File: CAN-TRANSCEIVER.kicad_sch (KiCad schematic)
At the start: 15 parts, among them IC2 ATA6561-GAQW-N

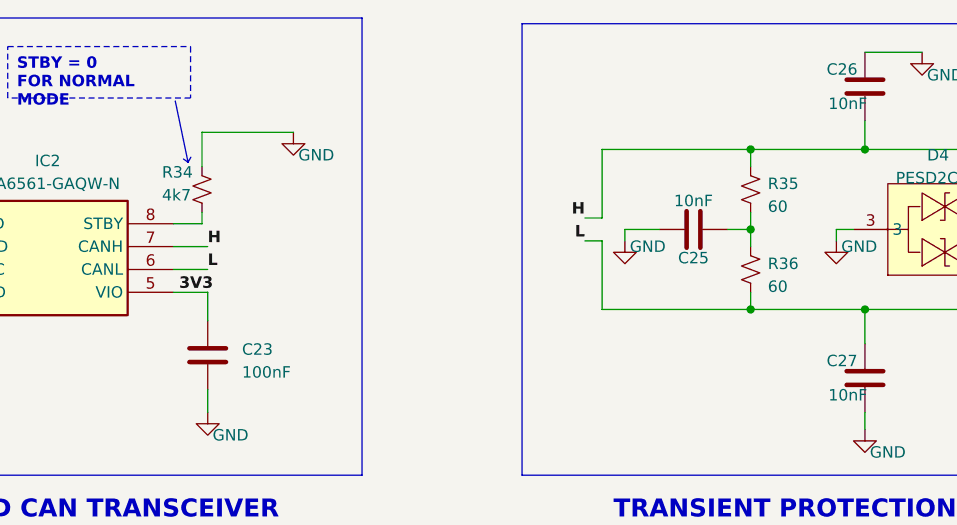
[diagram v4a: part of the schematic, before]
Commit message: Assigned footprints
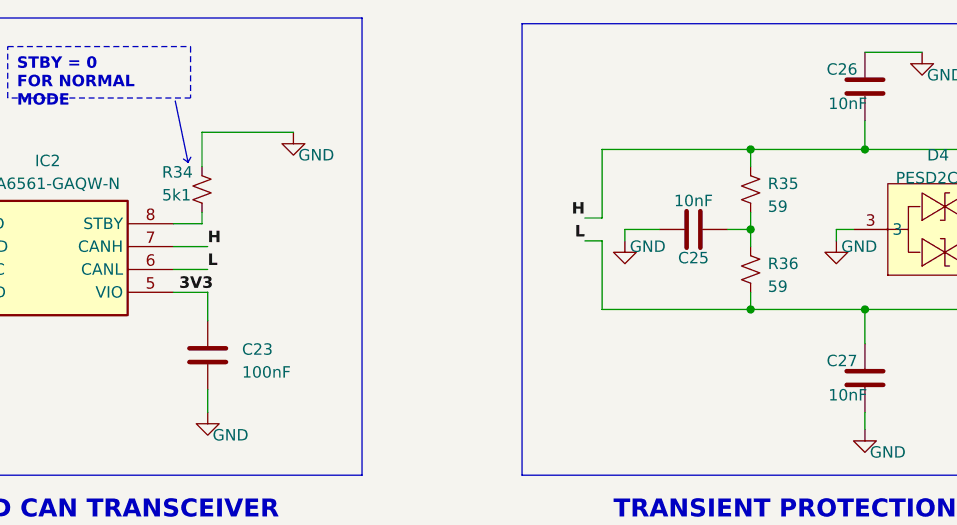
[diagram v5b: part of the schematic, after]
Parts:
- C23, C24, C25, C26, C27: footprint ESP32-S3_DB:C_0402_1005Metric -> ESP32-S3_Dev_Board:C_0402_1005Metric
- D4: footprint easyeda2kicad:SOT-23-3_L2.9-W1.3-P1.90-LS2.4-BR -> ESP32-S3_Dev_Board:SOT-23-3; PN (none) -> PESD2CAN
- IC2: footprint SOIC127P600X175-8N -> ESP32-S3_Dev_Board:SOP-8_3.9x4.9mm_P1.27mm; PN (none) -> ATA6561-GAQW-N
- R14: footprint (none) -> ESP32-S3_Dev_Board:R_0603_1608Metric; PN (none) -> RC0603JR-070RL
- R34: value 4k7 -> 5k1; footprint (none) -> ESP32-S3_Dev_Board:R_0402_1005Metric; PN (none) -> RC0402FR-075K1L
- R35, R36: value 60 -> 59; footprint (none) -> ESP32-S3_Dev_Board:R_0402_1005Metric; PN (none) -> RC0402FR-0759RL
- R37, R38: footprint (none) -> ESP32-S3_Dev_Board:R_0402_1005Metric; PN (none) -> RTT02100JTH
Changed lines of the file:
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@@
       (effects (font (size 1.27 1.27)) (justify left))
     )
-    (property "Footprint" "ESP32-S3_DB:C_0402_1005Metric" (at 167.3352 114.3 0)
+    (property "Footprint" "ESP32-S3_Dev_Board:C_0402_1005Metric" (at 167.3352 114.3 0)
       (effects (font (size 1.27 1.27)) hide)
     )
@@
       (effects (font (size 1.27 1.27)) (justify right))
     )
-    (property "Footprint" "ESP32-S3_DB:C_0402_1005Metric" (at 124.1552 106.68 0)
+    (property "Footprint" "ESP32-S3_Dev_Board:C_0402_1005Metric" (at 124.1552 106.68 0)
       (effects (font (size 1.27 1.27)) hide)
     )
@@
       (effects (font (size 1.27 1.27)) (justify right))
     )
-    (property "Value" "4k7" (at 161.29 92.71 0)
-      (effects (font (size 1.27 1.27)) (justify right))
-    )
-    (property "Footprint" "" (at 165.735 92.075 0)
+    (property "Value" "5k1" (at 161.29 92.71 0)
+      (effects (font (size 1.27 1.27)) (justify right))
+    )
+    (property "Footprint" "ESP32-S3_Dev_Board:R_0402_1005Metric" (at 165.735 92.075 0)
       (effects (font (size 1.27 1.27)) hide)
     )
@@
       (effects (font (size 1.27 1.27)) hide)
     )
+    (property "PN" "RC0402FR-075K1L" (at 165.735 92.075 0)
+      (effects (font (size 1.27 1.27)) hide)
+    )
     (pin "1")
     (pin "2")
@@
       (effects (font (size 1.27 1.27)))
     )
-    (property "Footprint" "ESP32-S3_DB:C_0402_1005Metric" (at 238.4298 76.835 0)
+    (property "Footprint" "ESP32-S3_Dev_Board:C_0402_1005Metric" (at 238.4298 76.835 0)
       (effects (font (size 1.27 1.27)) hide)
     )
@@
       (effects (font (size 1.27 1.27)))
     )
-    (property "Footprint" "" (at 131.445 100.965 0)
+    (property "Footprint" "ESP32-S3_Dev_Board:R_0603_1608Metric" (at 131.445 100.965 0)
       (effects (font (size 1.27 1.27)) hide)
     )
     (property "Datasheet" "~" (at 131.445 100.965 0)
+      (effects (font (size 1.27 1.27)) hide)
+    )
+    (property "PN" "RC0603JR-070RL" (at 131.445 100.965 0)
       (effects (font (size 1.27 1.27)) hide)
     )
@@
       (effects (font (size 1.27 1.27)) (justify right))
     )
-    (property "Value" "60" (at 228.6 102.87 0)
-      (effects (font (size 1.27 1.27)) (justify right))
-    )
-    (property "Footprint" "" (at 226.695 100.965 0)
+    (property "Value" "59" (at 228.6 102.87 0)
+      (effects (font (size 1.27 1.27)) (justify right))
+    )
+    (property "Footprint" "ESP32-S3_Dev_Board:R_0402_1005Metric" (at 226.695 100.965 0)
       (effects (font (size 1.27 1.27)) hide)
     )
     (property "Datasheet" "~" (at 226.695 100.965 0)
+      (effects (font (size 1.27 1.27)) hide)
+    )
+    (property "PN" "RC0402FR-0759RL" (at 226.695 100.965 0)
       (effects (font (size 1.27 1.27)) hide)
     )
@@
       (effects (font (size 1.27 1.27)))
     )
-    (property "Footprint" "SOIC127P600X175-8N" (at 158.75 190.805 0)
+    (property "Footprint" "ESP32-S3_Dev_Board:SOP-8_3.9x4.9mm_P1.27mm" (at 158.75 190.805 0)
       (effects (font (size 1.27 1.27)) (justify left top) hide)
     )
@@
     (property "Arrow Price/Stock" "https://www.arrow.com/en/products/ata6561-gaqw-n/microchip-technology?region=nac" (at 158.75 1090.805 0)
       (effects (font (size 1.27 1.27)) (justify left top) hide)
+    )
+    (property "PN" "ATA6561-GAQW-N" (at 134.62 95.885 0)
+      (effects (font (size 1.27 1.27)) hide)
     )
     (pin "1")
@@
       (effects (font (size 1.27 1.27)))
     )
-    (property "Footprint" "easyeda2kicad:SOT-23-3_L2.9-W1.3-P1.90-LS2.4-BR" (at 263.525 96.52 0)
+    (property "Footprint" "ESP32-S3_Dev_Board:SOT-23-3" (at 263.525 96.52 0)
       (effects (font (size 1.27 1.27)) hide)
     )
@@
     )
     (property "LCSC Part" "C284078" (at 268.605 96.52 0)
+      (effects (font (size 1.27 1.27)) hide)
+    )
+    (property "PN" "PESD2CAN" (at 248.285 96.52 0)
       (effects (font (size 1.27 1.27)) hide)
     )
@@
       (effects (font (size 1.27 1.27)) (justify right))
     )
-    (property "Footprint" "" (at 66.04 101.6 0)
+    (property "Footprint" "ESP32-S3_Dev_Board:R_0402_1005Metric" (at 66.04 101.6 0)
       (effects (font (size 1.27 1.27)) hide)
     )
@@
       (effects (font (size 1.27 1.27)) hide)
     )
+    (property "PN" "RTT02100JTH" (at 66.04 101.6 0)
+      (effects (font (size 1.27 1.27)) hide)
+    )
     (pin "1")
     (pin "2")
@@
       (effects (font (size 1.27 1.27)) (justify right))
     )
-    (property "Footprint" "" (at 66.04 95.25 0)
+    (property "Footprint" "ESP32-S3_Dev_Board:R_0402_1005Metric" (at 66.04 95.25 0)
       (effects (font (size 1.27 1.27)) hide)
     )
     (property "Datasheet" "~" (at 66.04 95.25 0)
+      (effects (font (size 1.27 1.27)) hide)
+    )
+    (property "PN" "RTT02100JTH" (at 66.04 95.25 0)
       (effects (font (size 1.27 1.27)) hide)
     )
@@
       (effects (font (size 1.27 1.27)) (justify right))
     )
-    (property "Value" "60" (at 228.6 93.98 0)
-      (effects (font (size 1.27 1.27)) (justify right))
-    )
-    (property "Footprint" "" (at 226.695 92.075 0)
+    (property "Value" "59" (at 228.6 93.98 0)
+      (effects (font (size 1.27 1.27)) (justify right))
+    )
+    (property "Footprint" "ESP32-S3_Dev_Board:R_0402_1005Metric" (at 226.695 92.075 0)
       (effects (font (size 1.27 1.27)) hide)
     )
@@
       (effects (font (size 1.27 1.27)) hide)
     )
+    (property "PN" "RC0402FR-0759RL" (at 226.695 92.075 0)
+      (effects (font (size 1.27 1.27)) hide)
+    )
     (pin "1")
     (pin "2")
@@
       (effects (font (size 1.27 1.27)))
     )
-    (property "Footprint" "ESP32-S3_DB:C_0402_1005Metric" (at 224.155 95.5548 0)
+    (property "Footprint" "ESP32-S3_Dev_Board:C_0402_1005Metric" (at 224.155 95.5548 0)
       (effects (font (size 1.27 1.27)) hide)
     )
@@
       (effects (font (size 1.27 1.27)))
     )
-    (property "Footprint" "ESP32-S3_DB:C_0402_1005Metric" (at 238.4298 109.22 0)
-      (effects (font (size 1.27 1.27)) hide)
-    )
+    (property "Footprint" "ESP32-S3_Dev_Board:C_0402_1005Metric" (at 238.4298 109.22 0)
+      (effects (font (size 1.27 1.27)) hide)
+    )

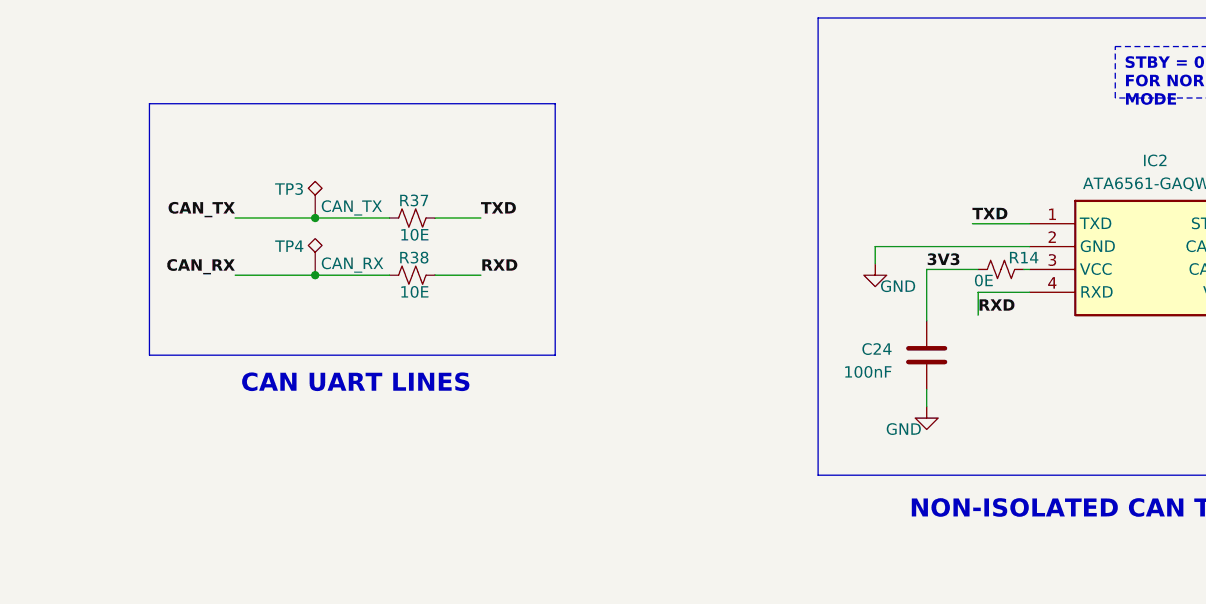
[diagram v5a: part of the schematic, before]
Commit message: Placed RS-485, CAN Transceiver and battery charger
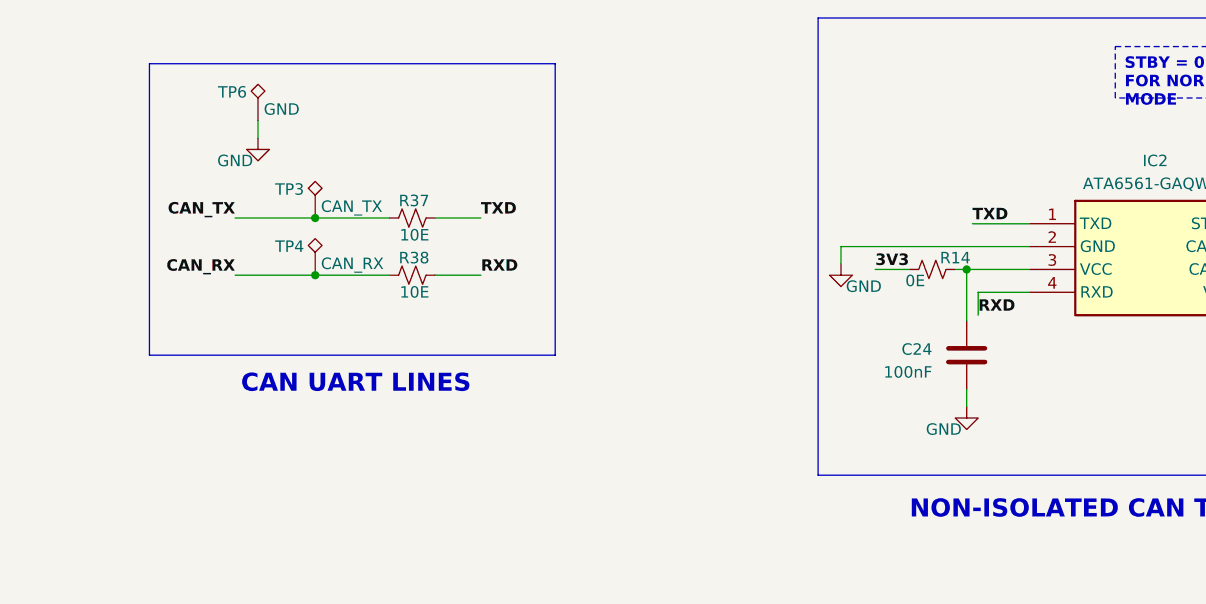
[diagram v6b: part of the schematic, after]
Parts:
- added TP6: GND, ESP32-S3_Dev_Board:Test_Pad_1.5mm, symbol ESP32-S3_DB:TestPoint_Alt
- TP3, TP4: footprint (none) -> ESP32-S3_Dev_Board:Test_Pad_1.5mm
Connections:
- net 3V3: no longer C24.2
- net GND: now also TP6.1
- net at IC2.3 (VCC), R14.2: now also C24.2
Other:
- moved on the sheet: C24, R14
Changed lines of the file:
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@@
   (junction (at 239.395 105.41) (diameter 0) (color 0 0 0 0)
   )
+  (junction (at 127.635 100.965) (diameter 0) (color 0 0 0 0)
+  )
   (junction (at 226.695 105.41) (diameter 0) (color 0 0 0 0)
   )
@@
     (stroke (width 1) (type default) (color 72 72 72 1))
   )
-  (wire (pts (xy 123.19 100.965) (xy 128.905 100.965))
+  (wire (pts (xy 117.475 100.965) (xy 121.285 100.965))
     (stroke (width 0) (type default))
   )
@@
     (stroke (width 0) (type default))
   )
-  (wire (pts (xy 123.19 114.3) (xy 123.19 116.205))
+  (wire (pts (xy 127.635 114.3) (xy 127.635 116.205))
     (stroke (width 0) (type default))
   )
@@
     (stroke (width 0) (type default))
   )
-  (bus (pts (xy 81.915 82.55) (xy 81.915 110.49))
+  (bus (pts (xy 81.915 78.105) (xy 81.915 110.49))
     (stroke (width 1) (type default) (color 72 72 72 1))
   )
@@
     (stroke (width 0) (type default))
   )
-  (wire (pts (xy 117.475 98.425) (xy 134.62 98.425))
+  (wire (pts (xy 113.665 98.425) (xy 134.62 98.425))
     (stroke (width 0) (type default))
   )
@@
     (stroke (width 0) (type default))
   )
-  (wire (pts (xy 133.985 100.965) (xy 134.62 100.965))
-    (stroke (width 0) (type default))
-  )
   (polyline (pts (xy 163.6776 88.6968) (xy 164.1856 89.0524))
     (stroke (width 0) (type default))
@@
     (stroke (width 0) (type default))
   )
-  (bus (pts (xy 36.83 82.55) (xy 81.915 82.55))
+  (bus (pts (xy 36.83 78.105) (xy 81.915 78.105))
     (stroke (width 1) (type default) (color 72 72 72 1))
   )
@@
     (stroke (width 0.5) (type default) (color 255 0 0 1))
   )
-  (bus (pts (xy 36.83 82.55) (xy 36.83 110.49))
+  (bus (pts (xy 36.83 78.105) (xy 36.83 110.49))
     (stroke (width 1) (type default) (color 72 72 72 1))
   )
@@
     (stroke (width 1) (type default) (color 72 72 72 1))
   )
-  (wire (pts (xy 117.475 100.33) (xy 117.475 98.425))
+  (wire (pts (xy 113.665 100.33) (xy 113.665 98.425))
     (stroke (width 0) (type default))
   )
@@
     (stroke (width 0) (type default))
   )
-  (wire (pts (xy 123.19 100.965) (xy 123.19 106.68))
+  (wire (pts (xy 127.635 100.965) (xy 134.62 100.965))
+    (stroke (width 0) (type default))
+  )
+  (wire (pts (xy 127.635 100.965) (xy 127.635 106.68))
     (stroke (width 0) (type default))
   )
@@
     (stroke (width 0) (type default))
   )
+  (wire (pts (xy 126.365 100.965) (xy 127.635 100.965))
+    (stroke (width 0) (type default))
+  )
   (wire (pts (xy 210.185 105.41) (xy 226.695 105.41))
     (stroke (width 0) (type default))
   )
   (wire (pts (xy 208.28 95.25) (xy 210.185 95.25))
+    (stroke (width 0) (type default))
+  )
+  (wire (pts (xy 48.895 86.36) (xy 48.895 84.455))
     (stroke (width 0) (type default))
   )
@@
     (effects (font (size 1.27 1.27) bold (color 0 0 255 1)) (justify left bottom))
   )
-  (label "3V3" (at 123.19 100.965 0) (fields_autoplaced)
+  (label "3V3" (at 117.475 100.965 0) (fields_autoplaced)
     (effects (font (size 1.27 1.27) bold (color 255 0 0 1)) (justify left bottom))
   )
@@
     )
   )
-  (symbol (lib_id "ESP32-S3_DB:C") (at 123.19 110.49 0) (mirror x) (unit 1)
-    (in_bom yes) (on_board yes) (dnp no)
-    (property "Reference" "C24" (at 119.38 109.855 0)
+  (symbol (lib_id "ESP32-S3_DB:C") (at 127.635 110.49 0) (mirror x) (unit 1)
+    (in_bom yes) (on_board yes) (dnp no)
+    (property "Reference" "C24" (at 123.825 109.855 0)
       (effects (font (size 1.27 1.27)) (justify right))
     )
-    (property "Value" "100nF" (at 119.38 112.395 0)
+    (property "Value" "100nF" (at 123.825 112.395 0)
       (effects (font (size 1.27 1.27)) (justify right))
     )
-    (property "Footprint" "ESP32-S3_Dev_Board:C_0402_1005Metric" (at 124.1552 106.68 0)
-      (effects (font (size 1.27 1.27)) hide)
-    )
-    (property "Datasheet" "~" (at 123.19 110.49 0)
-      (effects (font (size 1.27 1.27)) hide)
-    )
-    (property "PN" "EMK107B7104KAHT" (at 123.19 110.49 0)
+    (property "Footprint" "ESP32-S3_Dev_Board:C_0402_1005Metric" (at 128.6002 106.68 0)
+      (effects (font (size 1.27 1.27)) hide)
+    )
+    (property "Datasheet" "~" (at 127.635 110.49 0)
+      (effects (font (size 1.27 1.27)) hide)
+    )
+    (property "PN" "EMK107B7104KAHT" (at 127.635 110.49 0)
       (effects (font (size 1.27 1.27)) hide)
     )
@@
         (path "/b7fc4bd3-c219-4455-832b-8d795385dcf1/5968696a-d1c3-4df1-9868-cceeab327a7d"
           (reference "C24") (unit 1)
+        )
+      )
+    )
+  )
+  (symbol (lib_id "ESP32-S3_DB:GND") (at 48.895 86.36 0) (unit 1)
+    (in_bom yes) (on_board yes) (dnp no)
+    (property "Reference" "#PWR070" (at 48.895 92.71 0)
+      (effects (font (size 1.27 1.27)) hide)
+    )
+    (property "Value" "GND" (at 46.355 88.9 0)
+      (effects (font (size 1.27 1.27)))
+    )
+    (property "Footprint" "" (at 48.895 86.36 0)
+      (effects (font (size 1.27 1.27)) hide)
+    )
+    (property "Datasheet" "" (at 48.895 86.36 0)
+      (effects (font (size 1.27 1.27)) hide)
+    )
+    (pin "1")
+    (instances
+      (project "ESP32-S3_DB"
+        (path "/b7fc4bd3-c219-4455-832b-8d795385dcf1/5968696a-d1c3-4df1-9868-cceeab327a7d"
+          (reference "#PWR070") (unit 1)
         )
       )
@@
       (effects (font (size 1.27 1.27)) (justify left))
     )
-    (property "Footprint" "" (at 60.325 101.6 0)
+    (property "Footprint" "ESP32-S3_Dev_Board:Test_Pad_1.5mm" (at 60.325 101.6 0)
       (effects (font (size 1.27 1.27)) hide)
     )
@@
     )
   )
-  (symbol (lib_id "ESP32-S3_DB:R_Small_US") (at 131.445 100.965 90) (unit 1)
-    (in_bom yes) (on_board yes) (dnp no)
-    (property "Reference" "R14" (at 133.985 99.695 90)
-      (effects (font (size 1.27 1.27)))
-    )
-    (property "Value" "0E" (at 129.54 102.235 90)
-      (effects (font (size 1.27 1.27)))
-    )
-    (property "Footprint" "ESP32-S3_Dev_Board:R_0603_1608Metric" (at 131.445 100.965 0)
-      (effects (font (size 1.27 1.27)) hide)
-    )
-    (property "Datasheet" "~" (at 131.445 100.965 0)
-      (effects (font (size 1.27 1.27)) hide)
-    )
-    (property "PN" "RC0603JR-070RL" (at 131.445 100.965 0)
+  (symbol (lib_id "ESP32-S3_DB:R_Small_US") (at 123.825 100.965 90) (unit 1)
+    (in_bom yes) (on_board yes) (dnp no)
+    (property "Reference" "R14" (at 126.365 99.695 90)
+      (effects (font (size 1.27 1.27)))
+    )
+    (property "Value" "0E" (at 121.92 102.235 90)
+      (effects (font (size 1.27 1.27)))
+    )
+    (property "Footprint" "ESP32-S3_Dev_Board:R_0603_1608Metric" (at 123.825 100.965 0)
+      (effects (font (size 1.27 1.27)) hide)
+    )
+    (property "Datasheet" "~" (at 123.825 100.965 0)
+      (effects (font (size 1.27 1.27)) hide)
+    )
+    (property "PN" "RC0603JR-070RL" (at 123.825 100.965 0)
       (effects (font (size 1.27 1.27)) hide)
     )
@@
     )
   )
-  (symbol (lib_id "ESP32-S3_DB:GND") (at 123.19 116.205 0) (unit 1)
-    (in_bom yes) (on_board yes) (dnp no)
-    (property "Reference" "#PWR039" (at 123.19 122.555 0)
-      (effects (font (size 1.27 1.27)) hide)
-    )
-    (property "Value" "GND" (at 120.65 118.745 0)
-      (effects (font (size 1.27 1.27)))
-    )
-    (property "Footprint" "" (at 123.19 116.205 0)
-      (effects (font (size 1.27 1.27)) hide)
-    )
-    (property "Datasheet" "" (at 123.19 116.205 0)
+  (symbol (lib_id "ESP32-S3_DB:TestPoint_Alt") (at 48.895 84.455 0) (unit 1)
+    (in_bom yes) (on_board yes) (dnp no)
+    (property "Reference" "TP6" (at 44.45 81.28 0)
+      (effects (font (size 1.27 1.27)) (justify left))
+    )
+    (property "Value" "GND" (at 49.53 83.185 0)
+      (effects (font (size 1.27 1.27)) (justify left))
+    )
+    (property "Footprint" "ESP32-S3_Dev_Board:Test_Pad_1.5mm" (at 53.975 84.455 0)
+      (effects (font (size 1.27 1.27)) hide)
+    )
+    (property "Datasheet" "~" (at 53.975 84.455 0)
+      (effects (font (size 1.27 1.27)) hide)
+    )
+    (pin "1")
+    (instances
+      (project "ESP32-S3_DB"
+        (path "/b7fc4bd3-c219-4455-832b-8d795385dcf1/5968696a-d1c3-4df1-9868-cceeab327a7d"
+          (reference "TP6") (unit 1)
+        )
+      )
+    )
+  )
+  (symbol (lib_id "ESP32-S3_DB:GND") (at 127.635 116.205 0) (unit 1)
+    (in_bom yes) (on_board yes) (dnp no)
+    (property "Reference" "#PWR039" (at 127.635 122.555 0)
+      (effects (font (size 1.27 1.27)) hide)
+    )
+    (property "Value" "GND" (at 125.095 118.745 0)
+      (effects (font (size 1.27 1.27)))
+    )
+    (property "Footprint" "" (at 127.635 116.205 0)
+      (effects (font (size 1.27 1.27)) hide)
+    )
+    (property "Datasheet" "" (at 127.635 116.205 0)
       (effects (font (size 1.27 1.27)) hide)
     )
@@
     )
   )
-  (symbol (lib_id "ESP32-S3_DB:GND") (at 117.475 100.33 0) (unit 1)
-    (in_bom yes) (on_board yes) (dnp no)
-    (property "Reference" "#PWR046" (at 117.475 106.68 0)
-      (effects (font (size 1.27 1.27)) hide)
-    )
-    (property "Value" "GND" (at 120.015 102.87 0)
-      (effects (font (size 1.27 1.27)))
-    )
-    (property "Footprint" "" (at 117.475 100.33 0)
-      (effects (font (size 1.27 1.27)) hide)
-    )
-    (property "Datasheet" "" (at 117.475 100.33 0)
+  (symbol (lib_id "ESP32-S3_DB:GND") (at 113.665 100.33 0) (unit 1)
+    (in_bom yes) (on_board yes) (dnp no)
+    (property "Reference" "#PWR046" (at 113.665 106.68 0)
+      (effects (font (size 1.27 1.27)) hide)
+    )
+    (property "Value" "GND" (at 116.205 102.87 0)
+      (effects (font (size 1.27 1.27)))
+    )
+    (property "Footprint" "" (at 113.665 100.33 0)
+      (effects (font (size 1.27 1.27)) hide)
+    )
+    (property "Datasheet" "" (at 113.665 100.33 0)
       (effects (font (size 1.27 1.27)) hide)
     )
@@
       (effects (font (size 1.27 1.27)) (justify left))
     )
-    (property "Footprint" "" (at 60.325 95.25 0)
-      (effects (font (size 1.27 1.27)) hide)
-    )
+    (property "Footprint" "ESP32-S3_Dev_Board:Test_Pad_1.5mm" (at 60.325 95.25 0)
+      (effects (font (size 1.27 1.27)) hide)
+    )
